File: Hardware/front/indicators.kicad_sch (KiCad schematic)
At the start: 5 parts

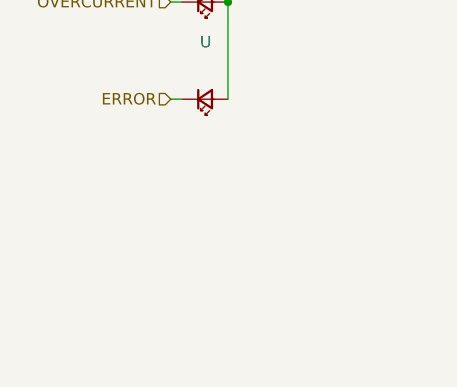
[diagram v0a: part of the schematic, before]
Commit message: Minor front panel tweaks
- Switched IO expander out for PCA9535 (easier to get replacement parts
  for, and (mostly) pin compatible with the XRA1200 we used before)

- Minor layout changes
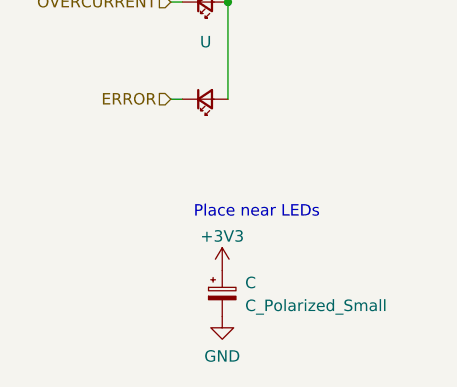
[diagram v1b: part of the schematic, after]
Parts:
- added C: C_Polarized_Small, symbol Device:C_Polarized_Small
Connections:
- net +3V3: now also C.1
- new net GND: C.2
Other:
- note added: "Place near LEDs"
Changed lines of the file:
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@@
     (stroke (width 0) (type default))
+  )
+  (text "Place near LEDs" (at 41.275 99.695 0)
+    (effects (font (size 1.27 1.27)) (justify left bottom))
   )
   (hierarchical_label "TRIGGER" (shape input) (at 38.735 53.975 180) (fields_autoplaced)
@@
     (pin "2")
   )
+  (symbol (lib_id "Device:C_Polarized_Small") (at 44.45 107.95 0) (unit 1)
+    (in_bom yes) (on_board yes) (fields_autoplaced)
+    (default_instance (reference "C") (unit 1) (value "C_Polarized_Small") (footprint ""))
+    (property "Reference" "C" (id 0) (at 46.99 106.7689 0)
+      (effects (font (size 1.27 1.27)) (justify left))
+    )
+    (property "Value" "C_Polarized_Small" (id 1) (at 46.99 109.3089 0)
+      (effects (font (size 1.27 1.27)) (justify left))
+    )
+    (property "Footprint" "" (id 2) (at 44.45 107.95 0)
+      (effects (font (size 1.27 1.27)) hide)
+    )
+    (property "Datasheet" "~" (id 3) (at 44.45 107.95 0)
+      (effects (font (size 1.27 1.27)) hide)
+    )
+    (pin "1")
+    (pin "2")
+  )
+  (symbol (lib_id "power:+3V3") (at 44.45 105.41 0) (unit 1)
+    (in_bom yes) (on_board yes) (fields_autoplaced)
+    (default_instance (reference "#PWR") (unit 1) (value "+3V3") (footprint ""))
+    (property "Reference" "#PWR" (id 0) (at 44.45 109.22 0)
+      (effects (font (size 1.27 1.27)) hide)
+    )
+    (property "Value" "+3V3" (id 1) (at 44.45 101.6 0)
+      (effects (font (size 1.27 1.27)))
+    )
+    (property "Footprint" "" (id 2) (at 44.45 105.41 0)
+      (effects (font (size 1.27 1.27)) hide)
+    )
+    (property "Datasheet" "" (id 3) (at 44.45 105.41 0)
+      (effects (font (size 1.27 1.27)) hide)
+    )
+    (pin "1")
+  )
   (symbol (lib_id "Device:LED_ARGB") (at 43.18 36.83 0) (unit 1)
     (in_bom yes) (on_board yes)
@@
     (pin "4")
   )
+  (symbol (lib_id "power:GND") (at 44.45 110.49 0) (unit 1)
+    (in_bom yes) (on_board yes)
+    (default_instance (reference "#PWR") (unit 1) (value "GND") (footprint ""))
+    (property "Reference" "#PWR" (id 0) (at 44.45 116.84 0)
+      (effects (font (size 1.27 1.27)) hide)
+    )
+    (property "Value" "GND" (id 1) (at 44.45 114.935 0)
+      (effects (font (size 1.27 1.27)))
+    )
+    (property "Footprint" "" (id 2) (at 44.45 110.49 0)
+      (effects (font (size 1.27 1.27)) hide)
+    )
+    (property "Datasheet" "" (id 3) (at 44.45 110.49 0)
+      (effects (font (size 1.27 1.27)) hide)
+    )
+    (pin "1")
+  )
   (symbol (lib_id "power:+3V3") (at 45.085 53.975 270) (unit 1)

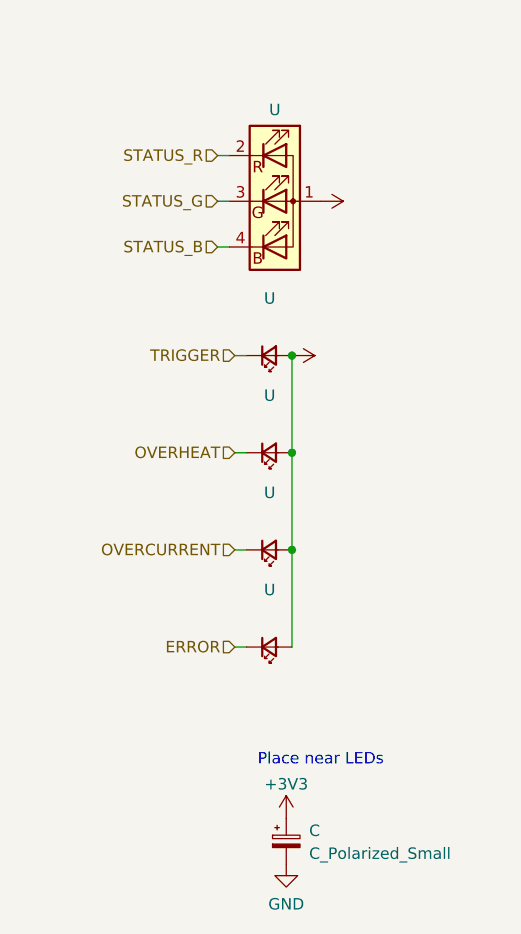
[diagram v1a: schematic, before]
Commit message: Rev4 front panel (#3)
* hw: start work on new front panel board

- This replaces all the various I2C chips with a single RP2040 (with
  some boot flash) to handle scanning the keyboard, driving PWM LEDs
  (including the display backlight) and actually handling the display
  controller initialization.

- Flipped the pinout of the connector to the main controller board

* hw: more front panel stuff

- fixed the mirrored pinout for the connector to the controller board

- Replaced a few capacitors to reduce BOM count

- Start connecting signals to RP2040, including the flash connection
  (dedicated to it)

* hw: First pass at new front panel

- Finished routing all signals on the front panel

- Put back the LED controller (PCA9955B) since that's a very nice and
  convenient way to drive the LEDs; it's driven via a "private" I2C bus
  from the RP2040 instead of the host controlling it.

  The touch panel controller is also hanging off this private bus so we
  can deal with it.

- Made trigger LED bicolor (green/orange)

* hw: minor front panel tweaks

* updated front panel pinout

- added system reset, direct load on/off switch output lines

- added separate touch screen reset/interrupt lines (the touch
  controller gets to be driven by linux side)

- update footprint for ER-TFT040-1 display

  this tweaks the sizes of the openings and the text labels a bit to be
  prettier

* swap touch irq/reset lines to match controller
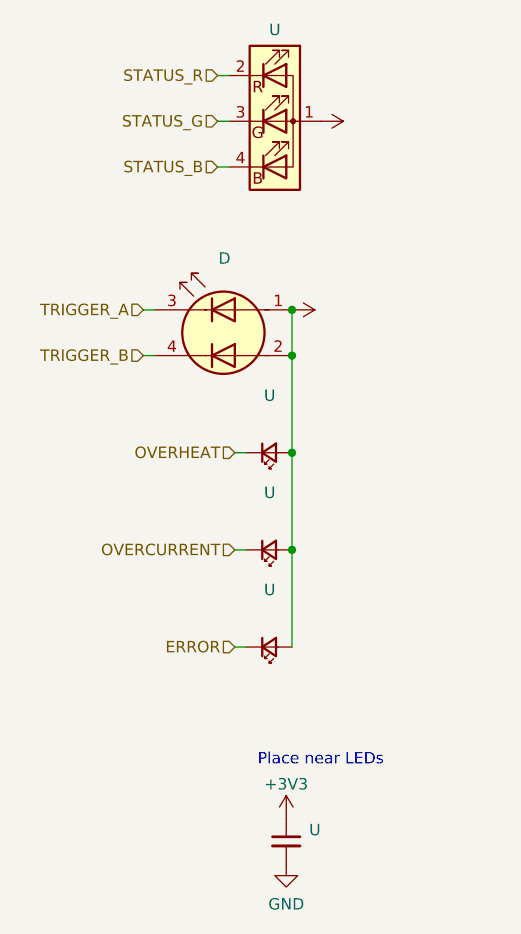
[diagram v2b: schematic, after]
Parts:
- removed C: C_Polarized_Small, symbol Device:C_Polarized_Small
- removed U: (no value), symbol Device:LED_Small
- added D: LED_Dual_AAKK, symbol Device:LED_Dual_AAKK
- added U: (no value), symbol Device:C_Small
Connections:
- net +3V3: now also D.1 (A1), D.2 (A2), U.1
- net GND: now also U.2
- new net TRIGGER_A: D.3 (K1)
- new net TRIGGER_B: D.4 (K2)
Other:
- moved on the sheet: U
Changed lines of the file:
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@@
   (title_block
     (title "Front Panel")
-    (date "2022-05-20")
-    (rev "2")
+    (date "2022-06-27")
+    (rev "4")
   )
   (junction (at 45.085 75.565) (diameter 0) (color 0 0 0 0)
@@
   (junction (at 45.085 53.975) (diameter 0) (color 0 0 0 0)
   )
+  (junction (at 45.085 48.895) (diameter 0) (color 0 0 0 0)
+  )
   (junction (at 45.085 64.77) (diameter 0) (color 0 0 0 0)
   )
@@
     (stroke (width 0) (type default))
   )
-  (wire (pts (xy 38.735 53.975) (xy 40.005 53.975))
-    (stroke (width 0) (type default))
-  )
   (wire (pts (xy 38.735 64.77) (xy 40.005 64.77))
     (stroke (width 0) (type default))
   )
-  (wire (pts (xy 36.83 41.91) (xy 38.1 41.91))
-    (stroke (width 0) (type default))
-  )
-  (wire (pts (xy 36.83 31.75) (xy 38.1 31.75))
+  (wire (pts (xy 36.83 33.02) (xy 38.1 33.02))
+    (stroke (width 0) (type default))
+  )
+  (wire (pts (xy 45.085 48.895) (xy 45.085 53.975))
+    (stroke (width 0) (type default))
+  )
+  (wire (pts (xy 36.83 22.86) (xy 38.1 22.86))
     (stroke (width 0) (type default))
   )
@@
     (stroke (width 0) (type default))
   )
+  (wire (pts (xy 28.575 48.895) (xy 29.845 48.895))
+    (stroke (width 0) (type default))
+  )
   (wire (pts (xy 45.085 53.975) (xy 45.085 64.77))
     (stroke (width 0) (type default))
   )
-  (wire (pts (xy 36.83 36.83) (xy 38.1 36.83))
+  (wire (pts (xy 28.575 53.975) (xy 29.845 53.975))
+    (stroke (width 0) (type default))
+  )
+  (wire (pts (xy 36.83 27.94) (xy 38.1 27.94))
     (stroke (width 0) (type default))
   )
@@
     (effects (font (size 1.27 1.27)) (justify left bottom))
   )
-  (hierarchical_label "TRIGGER" (shape input) (at 38.735 53.975 180) (fields_autoplaced)
-    (effects (font (size 1.27 1.27)) (justify right))
-  )
   (hierarchical_label "ERROR" (shape input) (at 38.735 86.36 180) (fields_autoplaced)
     (effects (font (size 1.27 1.27)) (justify right))
   )
-  (hierarchical_label "STATUS_B" (shape input) (at 36.83 41.91 180) (fields_autoplaced)
+  (hierarchical_label "STATUS_B" (shape input) (at 36.83 33.02 180) (fields_autoplaced)
+    (effects (font (size 1.27 1.27)) (justify right))
+  )
+  (hierarchical_label "TRIGGER_A" (shape input) (at 28.575 48.895 180) (fields_autoplaced)
     (effects (font (size 1.27 1.27)) (justify right))
   )
@@
     (effects (font (size 1.27 1.27)) (justify right))
   )
-  (hierarchical_label "STATUS_G" (shape input) (at 36.83 36.83 180) (fields_autoplaced)
+  (hierarchical_label "TRIGGER_B" (shape input) (at 28.575 53.975 180) (fields_autoplaced)
+    (effects (font (size 1.27 1.27)) (justify right))
+  )
+  (hierarchical_label "STATUS_G" (shape input) (at 36.83 27.94 180) (fields_autoplaced)
     (effects (font (size 1.27 1.27)) (justify right))
   )
@@
     (effects (font (size 1.27 1.27)) (justify right))
   )
-  (hierarchical_label "STATUS_R" (shape input) (at 36.83 31.75 180) (fields_autoplaced)
+  (hierarchical_label "STATUS_R" (shape input) (at 36.83 22.86 180) (fields_autoplaced)
     (effects (font (size 1.27 1.27)) (justify right))
   )
@@
     (pin "2")
   )
-  (symbol (lib_id "power:+3V3") (at 48.26 36.83 270) (unit 1)
-    (in_bom yes) (on_board yes)
-    (default_instance (reference "U") (unit 1) (value "") (footprint ""))
-    (property "Reference" "U" (id 0) (at 44.45 36.83 0)
-      (effects (font (size 1.27 1.27)) hide)
-    )
-    (property "Value" "" (id 1) (at 51.435 36.83 90)
-      (effects (font (size 1.27 1.27)) (justify left))
-    )
-    (property "Footprint" "" (id 2) (at 48.26 36.83 0)
-      (effects (font (size 1.27 1.27)) hide)
-    )
-    (property "Datasheet" "" (id 3) (at 48.26 36.83 0)
-      (effects (font (size 1.27 1.27)) hide)
-    )
-    (pin "1")
-  )
-  (symbol (lib_id "Device:LED_Small") (at 42.545 53.975 0) (mirror x) (unit 1)
-    (in_bom yes) (on_board yes) (fields_autoplaced)
-    (default_instance (reference "U") (unit 1) (value "") (footprint ""))
-    (property "Reference" "U" (id 0) (at 42.6085 47.625 0)
-      (effects (font (size 1.27 1.27)))
-    )
-    (property "Value" "" (id 1) (at 42.6085 50.165 0)
-      (effects (font (size 1.27 1.27)))
-    )
-    (property "Footprint" "" (id 2) (at 42.545 53.975 90)
-      (effects (font (size 1.27 1.27)) hide)
-    )
-    (property "Datasheet" "~" (id 3) (at 42.545 53.975 90)
-      (effects (font (size 1.27 1.27)) hide)
-    )
-    (property "MPN" "156120VS82500" (id 4) (at 42.545 53.975 0)
-      (effects (font (size 1.27 1.27)) hide)
-    )
-    (pin "1")
-    (pin "2")
+  (symbol (lib_id "Device:LED_Dual_AAKK") (at 37.465 51.435 0) (mirror y) (unit 1)
+    (in_bom yes) (on_board yes)
+    (default_instance (reference "D") (unit 1) (value "LED_Dual_AAKK") (footprint ""))
+    (property "Reference" "D" (id 0) (at 37.592 43.18 0)
+      (effects (font (size 1.27 1.27)))
+    )
+    (property "Value" "LED_Dual_AAKK" (id 1) (at 37.592 43.18 0)
+      (effects (font (size 1.27 1.27)) hide)
+    )
+    (property "Footprint" "" (id 2) (at 36.703 51.435 0)
+      (effects (font (size 1.27 1.27)) hide)
+    )
+    (property "Datasheet" "~" (id 3) (at 36.703 51.435 0)
+      (effects (font (size 1.27 1.27)) hide)
+    )
+    (property "MPN" "LTST-C155KGKFKT" (id 4) (at 37.465 51.435 0)
+      (effects (font (size 1.27 1.27)) hide)
+    )
+    (pin "1")
+    (pin "2")
+    (pin "3")
+    (pin "4")
+  )
+  (symbol (lib_id "power:+3V3") (at 48.26 27.94 270) (unit 1)
+    (in_bom yes) (on_board yes)
+    (default_instance (reference "U") (unit 1) (value "") (footprint ""))
+    (property "Reference" "U" (id 0) (at 44.45 27.94 0)
+      (effects (font (size 1.27 1.27)) hide)
+    )
+    (property "Value" "" (id 1) (at 51.435 27.94 90)
+      (effects (font (size 1.27 1.27)) (justify left))
+    )
+    (property "Footprint" "" (id 2) (at 48.26 27.94 0)
+      (effects (font (size 1.27 1.27)) hide)
+    )
+    (property "Datasheet" "" (id 3) (at 48.26 27.94 0)
+      (effects (font (size 1.27 1.27)) hide)
+    )
+    (pin "1")
   )
   (symbol (lib_id "Device:LED_Small") (at 42.545 64.77 0) (mirror x) (unit 1)
@@
     (pin "2")
   )
-  (symbol (lib_id "Device:C_Polarized_Small") (at 44.45 107.95 0) (unit 1)
-    (in_bom yes) (on_board yes) (fields_autoplaced)
-    (default_instance (reference "C") (unit 1) (value "C_Polarized_Small") (footprint ""))
-    (property "Reference" "C" (id 0) (at 46.99 106.7689 0)
-      (effects (font (size 1.27 1.27)) (justify left))
-    )
-    (property "Value" "C_Polarized_Small" (id 1) (at 46.99 109.3089 0)
+  (symbol (lib_id "Device:C_Small") (at 44.45 107.95 0) (unit 1)
+    (in_bom yes) (on_board yes) (fields_autoplaced)
+    (default_instance (reference "U") (unit 1) (value "") (footprint ""))
+    (property "Reference" "U" (id 0) (at 46.99 106.6862 0)
+      (effects (font (size 1.27 1.27)) (justify left))
+    )
+    (property "Value" "" (id 1) (at 46.99 109.2262 0)
       (effects (font (size 1.27 1.27)) (justify left))
     )
@@
     )
     (property "Datasheet" "~" (id 3) (at 44.45 107.95 0)
+      (effects (font (size 1.27 1.27)) hide)
+    )
+    (property "MPN" "" (id 4) (at 44.45 107.95 0)
+      (effects (font (size 1.27 1.27)) hide)
+    )
+    (property "JLCPCB" "C19666" (id 5) (at 44.45 107.95 0)
       (effects (font (size 1.27 1.27)) hide)
     )
@@
     (pin "1")
   )
-  (symbol (lib_id "Device:LED_ARGB") (at 43.18 36.83 0) (unit 1)
-    (in_bom yes) (on_board yes)
-    (default_instance (reference "U") (unit 1) (value "") (footprint ""))
-    (property "Reference" "U" (id 0) (at 43.18 26.67 0)
-      (effects (font (size 1.27 1.27)))
-    )
-    (property "Value" "" (id 1) (at 43.18 26.035 0)
-      (effects (font (size 1.27 1.27)) hide)
-    )
-    (property "Footprint" "" (id 2) (at 43.18 38.1 0)
-      (effects (font (size 1.27 1.27)) hide)
-    )
-    (property "Datasheet" "~" (id 3) (at 43.18 38.1 0)
-      (effects (font (size 1.27 1.27)) hide)
-    )
-    (property "MPN" "IN-S128TATRGB" (id 4) (at 43.18 36.83 0)
+  (symbol (lib_id "Device:LED_ARGB") (at 43.18 27.94 0) (unit 1)
+    (in_bom yes) (on_board yes)
+    (default_instance (reference "U") (unit 1) (value "") (footprint ""))
+    (property "Reference" "U" (id 0) (at 43.18 17.78 0)
+      (effects (font (size 1.27 1.27)))
+    )
+    (property "Value" "" (id 1) (at 43.18 17.145 0)
+      (effects (font (size 1.27 1.27)) hide)
+    )
+    (property "Footprint" "" (id 2) (at 43.18 29.21 0)
+      (effects (font (size 1.27 1.27)) hide)
+    )
+    (property "Datasheet" "~" (id 3) (at 43.18 29.21 0)
+      (effects (font (size 1.27 1.27)) hide)
+    )
+    (property "MPN" "IN-S128TATRGB" (id 4) (at 43.18 27.94 0)
       (effects (font (size 1.27 1.27)) hide)
     )
@@
     (pin "1")
   )
-  (symbol (lib_id "power:+3V3") (at 45.085 53.975 270) (unit 1)
-    (in_bom yes) (on_board yes) (fields_autoplaced)
-    (default_instance (reference "U") (unit 1) (value "") (footprint ""))
-    (property "Reference" "U" (id 0) (at 41.275 53.975 0)
-      (effects (font (size 1.27 1.27)) hide)
-    )
-    (property "Value" "" (id 1) (at 48.895 53.9749 90)
-      (effects (font (size 1.27 1.27)) (justify left))
-    )
-    (property "Footprint" "" (id 2) (at 45.085 53.975 0)
-      (effects (font (size 1.27 1.27)) hide)
-    )
-    (property "Datasheet" "" (id 3) (at 45.085 53.975 0)
-      (effects (font (size 1.27 1.27)) hide)
-    )
+  (symbol (lib_id "power:+3V3") (at 45.085 48.895 270) (unit 1)
+    (in_bom yes) (on_board yes) (fields_autoplaced)
+    (default_instance (reference "U") (unit 1) (value "") (footprint ""))
+    (property "Reference" "U" (id 0) (at 41.275 48.895 0)
+      (effects (font (size 1.27 1.27)) hide)
+    )
+    (property "Value" "" (id 1) (at 48.895 48.8949 90)
+      (effects (font (size 1.27 1.27)) (justify left))
+    )
+    (property "Footprint" "" (id 2) (at 45.085 48.895 0)
+      (effects (font (size 1.27 1.27)) hide)
+    )
+    (property "Datasheet" "" (id 3) (at 45.085 48.895 0)
+      (effects (font (size 1.27 1.27)) hide)
+    )

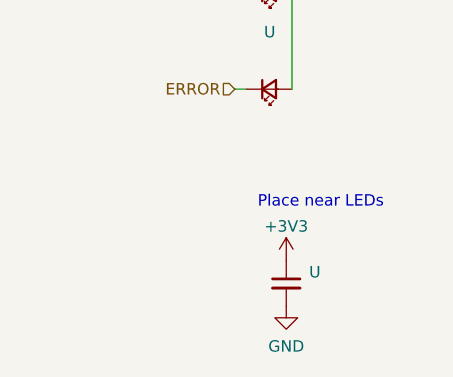
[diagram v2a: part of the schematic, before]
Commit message: front: minor tweaks
- added some more pull-ups on IO lines

- doubled decoupling capacitance for LEDs
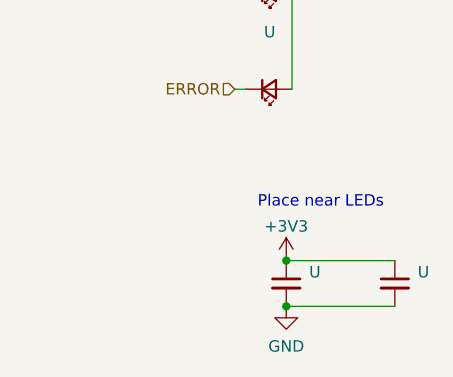
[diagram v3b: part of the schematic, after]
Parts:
- added U: (no value), symbol Device:C_Small
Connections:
- net +3V3: now also U.1
- net GND: now also U.2
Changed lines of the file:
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@@
   (junction (at 45.085 75.565) (diameter 0) (color 0 0 0 0)
   )
+  (junction (at 44.45 105.41) (diameter 0) (color 0 0 0 0)
+  )
   (junction (at 45.085 53.975) (diameter 0) (color 0 0 0 0)
+  )
+  (junction (at 44.45 110.49) (diameter 0) (color 0 0 0 0)
   )
   (junction (at 45.085 48.895) (diameter 0) (color 0 0 0 0)
@@
   )
   (wire (pts (xy 36.83 33.02) (xy 38.1 33.02))
+    (stroke (width 0) (type default))
+  )
+  (wire (pts (xy 44.45 105.41) (xy 56.515 105.41))
     (stroke (width 0) (type default))
   )
@@
   )
   (wire (pts (xy 36.83 27.94) (xy 38.1 27.94))
+    (stroke (width 0) (type default))
+  )
+  (wire (pts (xy 44.45 110.49) (xy 56.515 110.49))
     (stroke (width 0) (type default))
   )
@@
       (effects (font (size 1.27 1.27)) hide)
     )
+    (pin "1")
+    (pin "2")
+  )
+  (symbol (lib_id "Device:C_Small") (at 56.515 107.95 0) (unit 1)
+    (in_bom yes) (on_board yes) (fields_autoplaced)
+    (default_instance (reference "U") (unit 1) (value "") (footprint ""))
+    (property "Reference" "U" (id 0) (at 59.055 106.6862 0)
+      (effects (font (size 1.27 1.27)) (justify left))
+    )
+    (property "Value" "" (id 1) (at 59.055 109.2262 0)
+      (effects (font (size 1.27 1.27)) (justify left))
+    )
+    (property "Footprint" "" (id 2) (at 56.515 107.95 0)
+      (effects (font (size 1.27 1.27)) hide)
+    )
+    (property "Datasheet" "~" (id 3) (at 56.515 107.95 0)
+      (effects (font (size 1.27 1.27)) hide)
+    )
+    (property "MPN" "" (id 4) (at 56.515 107.95 0)
+      (effects (font (size 1.27 1.27)) hide)
+    )
+    (property "JLCPCB" "C19666" (id 5) (at 56.515 107.95 0)
+      (effects (font (size 1.27 1.27)) hide)
+    )
